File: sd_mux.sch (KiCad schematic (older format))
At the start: 8 parts, among them IC1 SN74CBT3257DR, IC2 SN74CBT3257DR, J1 Micro_SD_Card_Det, J2 DEVICE 1, J3 DEVICE 2, J4 CONTROL

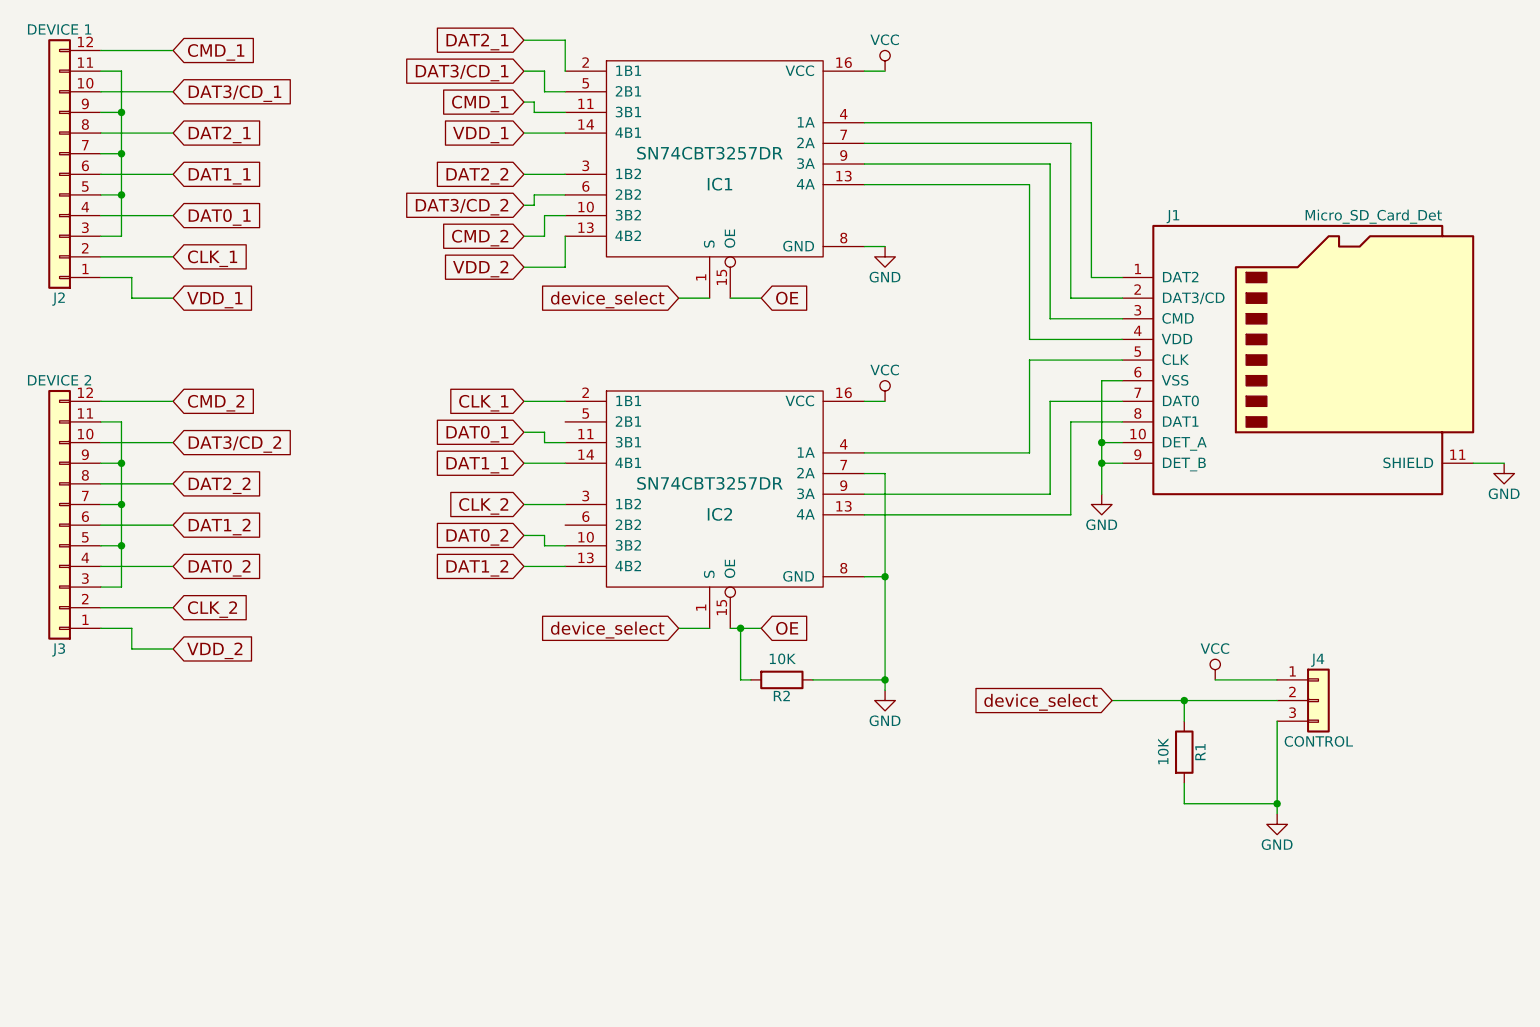
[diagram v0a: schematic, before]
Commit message: added some additional passives, fixed mistakes
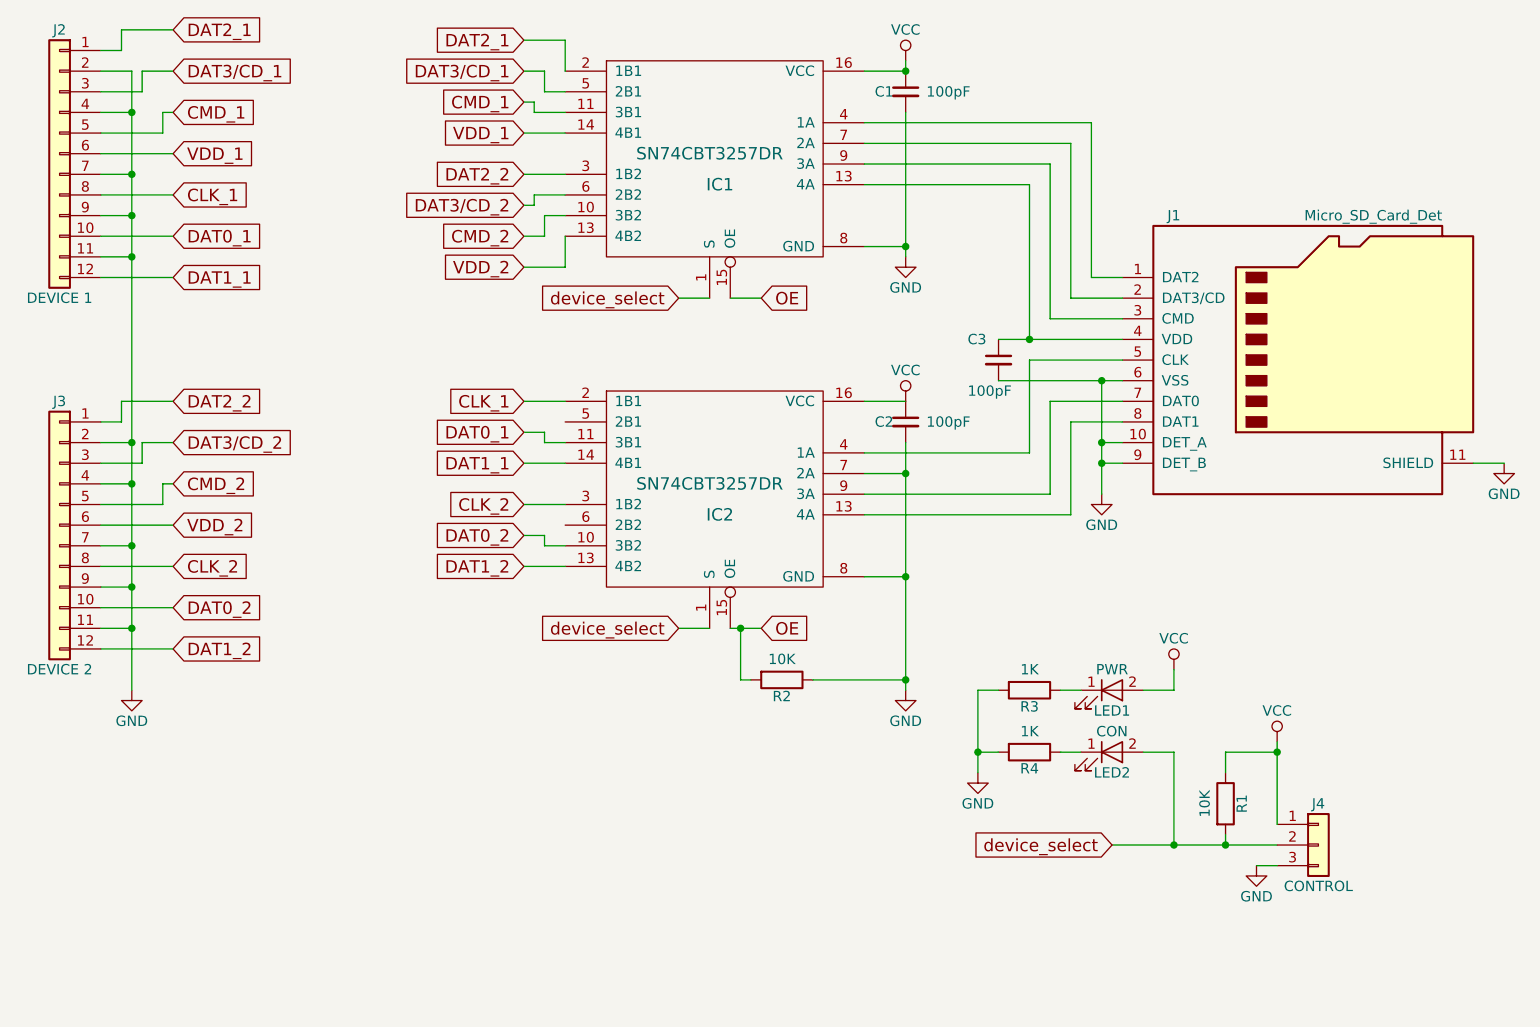
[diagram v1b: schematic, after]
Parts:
- added C1, C2, C3: 100pF, symbol C_Small
- added CON: LED2, symbol LED
- added PWR: LED1, symbol LED
- added R3, R4: 1K, symbol R
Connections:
- net CLK_1: now also J2.8 (Pin_8); no longer J2.2 (Pin_2)
- net CLK_2: now also J3.8 (Pin_8); no longer J3.2 (Pin_2)
- net CMD_1: now also J2.5 (Pin_5); no longer J2.12 (Pin_12)
- net CMD_2: now also J3.5 (Pin_5); no longer J3.12 (Pin_12)
- net DAT0_1: now also J2.10 (Pin_10); no longer J2.4 (Pin_4)
- net DAT0_2: now also J3.10 (Pin_10); no longer J3.4 (Pin_4)
- net DAT1_1: now also J2.12 (Pin_12); no longer J2.6 (Pin_6)
- net DAT1_2: now also J3.12 (Pin_12); no longer J3.6 (Pin_6)
- net DAT2_1: now also J2.1 (Pin_1); no longer J2.8 (Pin_8)
- net DAT2_2: now also J3.1 (Pin_1); no longer J3.8 (Pin_8)
- net DAT3/CD_1: now also J2.3 (Pin_3); no longer J2.10 (Pin_10)
- net DAT3/CD_2: now also J3.3 (Pin_3); no longer J3.10 (Pin_10)
- net GND: now also J2.11 (Pin_11), J2.2 (Pin_2), J2.4 (Pin_4), J2.7 (Pin_7), J2.9 (Pin_9), J3.11 (Pin_11), J3.2 (Pin_2), J3.4 (Pin_4), J3.7 (Pin_7), J3.9 (Pin_9), C1.2, C2.2, C3.2, R3.2, R4.2; no longer R1.2
- net VCC: now also R1.1, C1.1, C2.1, PWR.2 (A)
- net VDD_1: now also J2.6 (Pin_6); no longer J2.1 (Pin_1)
- net VDD_2: now also J3.6 (Pin_6); no longer J3.1 (Pin_1)
- net device_select: now also R1.2, CON.2 (A); no longer R1.1
- net at IC1.13 (4B2), J1.4 (VDD): now also C3.1
- new net: PWR.1 (K), R3.1
- new net: CON.1 (K), R4.1
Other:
- moved on the sheet: J3, J4, R1

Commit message: fix warnings, adjust component values
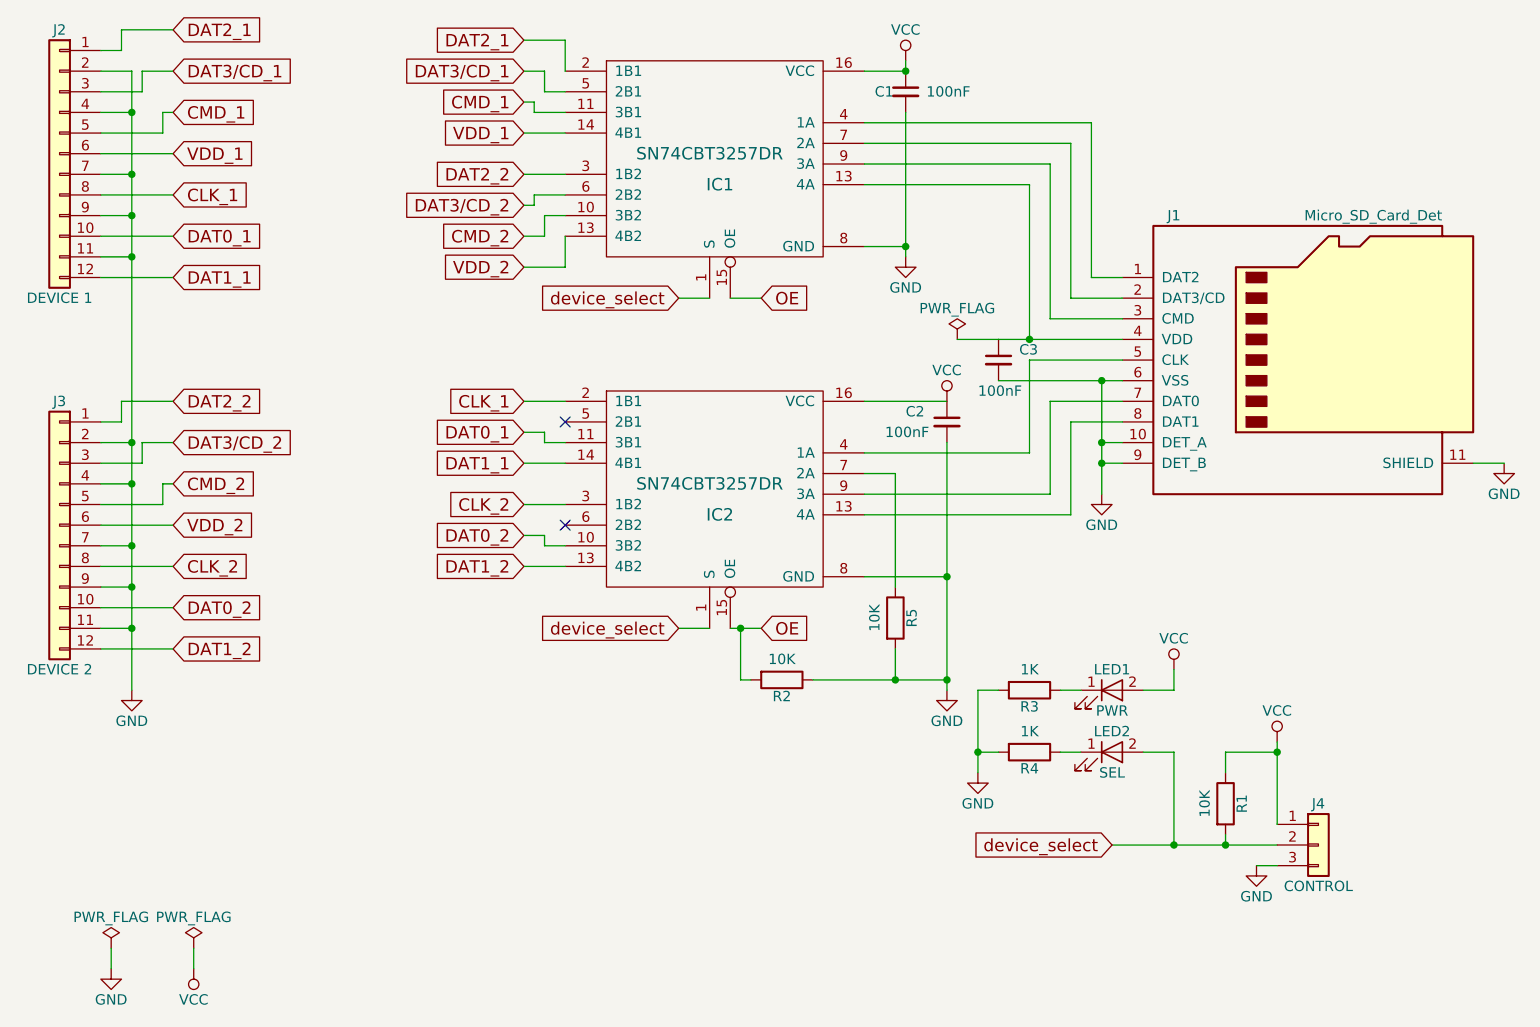
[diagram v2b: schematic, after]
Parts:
- removed CON: LED2, symbol LED
- removed PWR: LED1, symbol LED
- added LED1: PWR, symbol LED
- added LED2: SEL, symbol LED
- added R5: 10K, symbol R
- C1, C2, C3: value 100pF -> 100nF
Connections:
- net GND: now also R5.2; no longer IC2.7 (2A)
- net VCC: now also LED1.2 (A)
- net device_select: now also LED2.2 (A)
- net at R3.1: now also LED1.1 (K)
- net at R4.1: now also LED2.1 (K)
- new net: IC2.7 (2A), R5.1
- no-connect marks 0 -> 2
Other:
- moved on the sheet: C2
